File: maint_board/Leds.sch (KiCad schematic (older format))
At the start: 20 parts

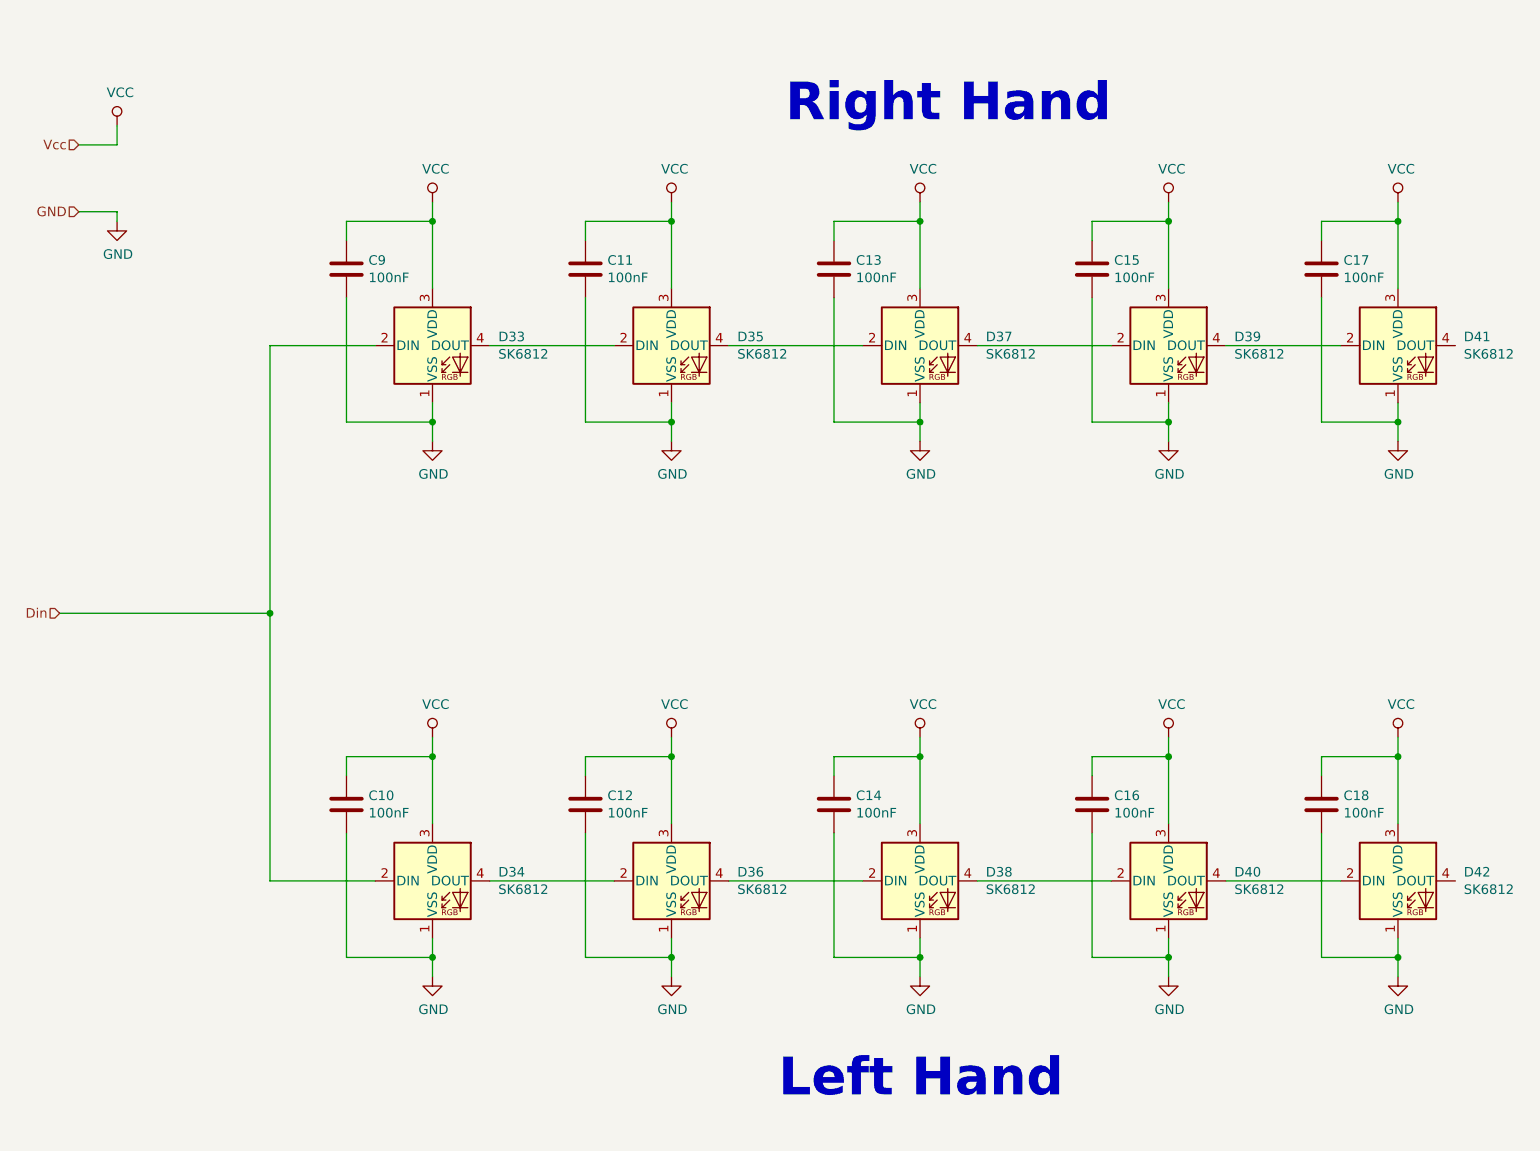
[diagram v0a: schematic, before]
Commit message: removed two leds and fixed recet and usb port
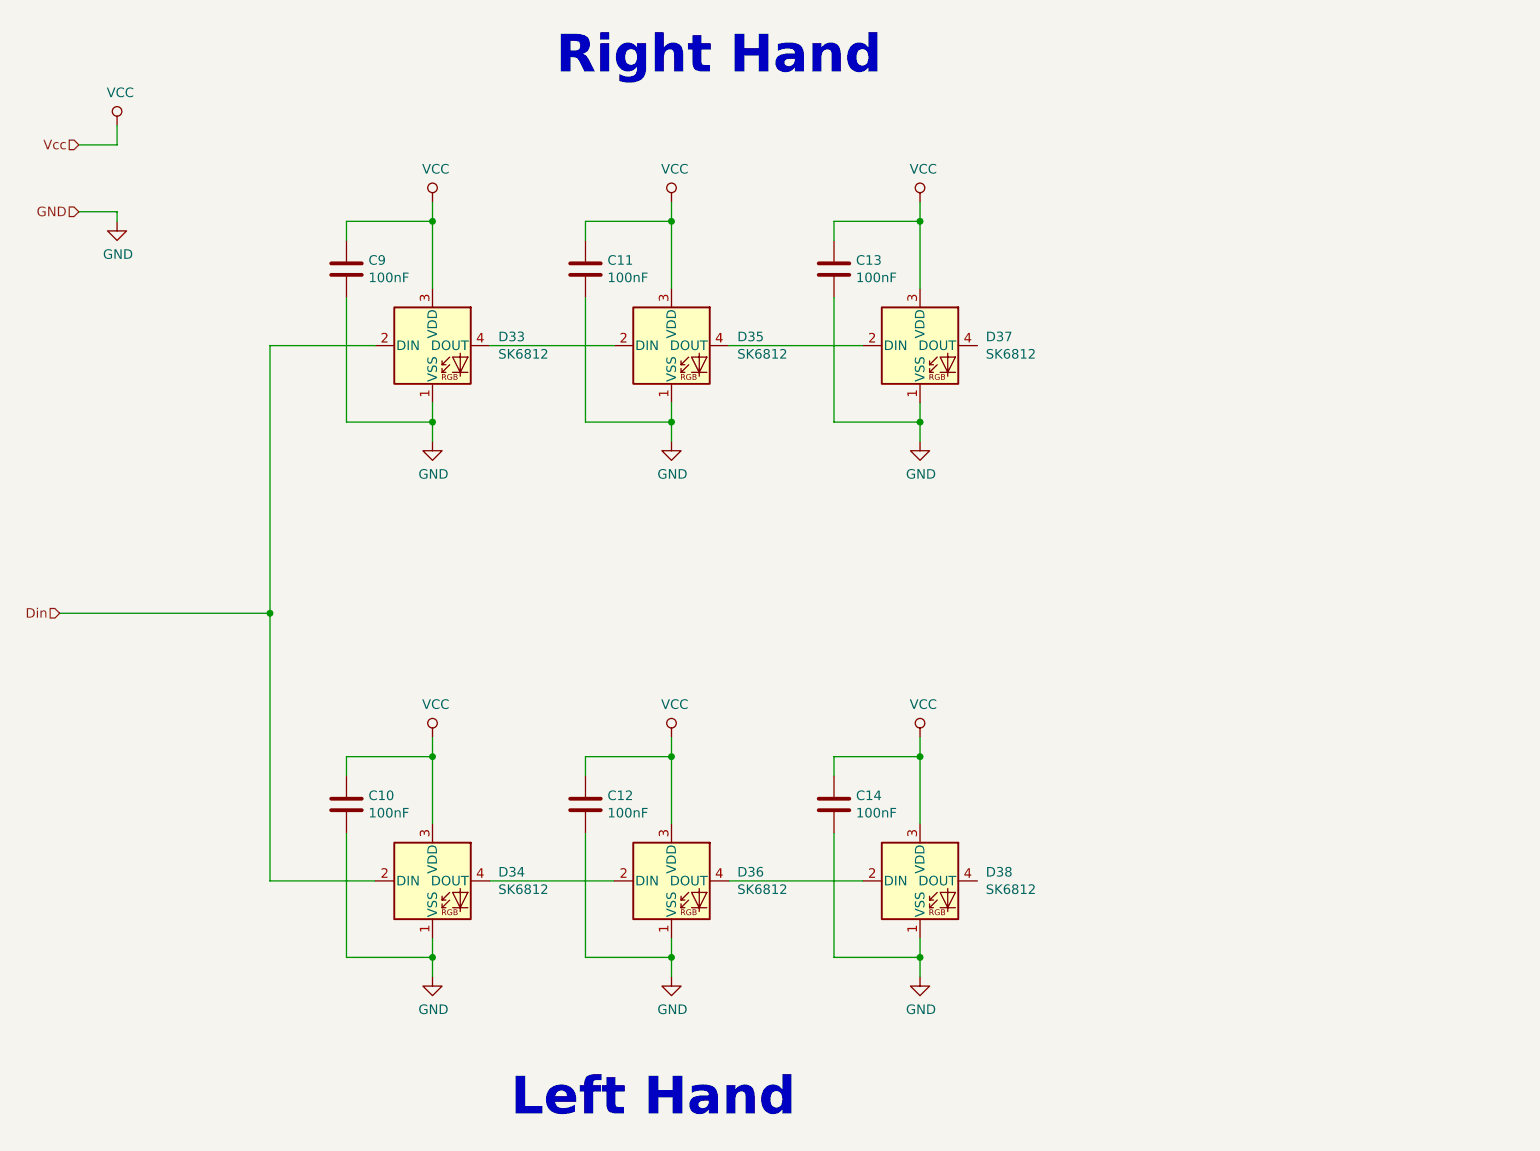
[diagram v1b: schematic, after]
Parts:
- removed C15, C16, C17, C18: 100nF, keyboard_parts:C_1608, symbol Device:C
- removed D39, D40, D41, D42: SK6812, LED_SMD:LED_SK6812_PLCC4_5.0x5.0mm_P3.2mm, symbol LED:SK6812

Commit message: this is before I switch to usb C
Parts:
- removed C13, C14: 100nF, keyboard_parts:C_1608, symbol Device:C
- removed D37, D38: SK6812, LED_SMD:LED_SK6812_PLCC4_5.0x5.0mm_P3.2mm, symbol LED:SK6812
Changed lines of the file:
@@
 $Descr A4 11693 8268
 encoding utf-8
-Sheet 4 4
+Sheet 3 4
 Title ""
 Date ""
@@
 F 3 "https://cdn-shop.adafruit.com/product-files/1138/SK6812+LED+datasheet+.pdf" H 4700 4925 50  0001 L TNN
 	1    4600 5300
-	1    0    0    -1
-$EndComp
-$Comp
-L LED:SK6812 D38
-U 1 1 6020E8F9
-P 5900 5300
-F 0 "D38" H 6244 5346 50  0000 L CNN
-F 1 "SK6812" H 6244 5255 50  0000 L CNN
-F 2 "LED_SMD:LED_SK6812_PLCC4_5.0x5.0mm_P3.2mm" H 5950 5000 50  0001 L TNN
-F 3 "https://cdn-shop.adafruit.com/product-files/1138/SK6812+LED+datasheet+.pdf" H 6000 4925 50  0001 L TNN
-	1    5900 5300
 	1    0    0    -1
 $EndComp
@@
 Wire Wire Line
 	3650 5300 4300 5300
-Wire Wire Line
-	4900 5300 5600 5300
 Text HLabel 1400 3900 0    50   Input ~ 0
 Din
@@
 $EndComp
 $Comp
-L power:VCC #PWR?
-U 1 1 602548C6
-P 5900 4550
-AR Path="/602548C6" Ref="#PWR?"  Part="1"
-AR Path="/6012B71A/602548C6" Ref="#PWR?"  Part="1"
-AR Path="/601EDEE5/602548C6" Ref="#PWR040"  Part="1"
-F 0 "#PWR040" H 5900 4400 50  0001 C CNN
-F 1 "VCC" H 5917 4723 50  0000 C CNN
-F 2 "" H 5900 4550 50  0001 C CNN
-F 3 "" H 5900 4550 50  0001 C CNN
-	1    5900 4550
-	1    0    0    -1
-$EndComp
-$Comp
 L power:GND #PWR?
 U 1 1 6025FF9C
@@
 	1    0    0    -1
 $EndComp
-$Comp
-L power:GND #PWR?
-U 1 1 6025FFA8
-P 5900 5800
-AR Path="/6025FFA8" Ref="#PWR?"  Part="1"
-AR Path="/6012B71A/6025FFA8" Ref="#PWR?"  Part="1"
-AR Path="/601EDEE5/6025FFA8" Ref="#PWR041"  Part="1"
-F 0 "#PWR041" H 5900 5550 50  0001 C CNN
-F 1 "GND" H 5905 5627 50  0000 C CNN
-F 2 "" H 5900 5800 50  0001 C CNN
-F 3 "" H 5900 5800 50  0001 C CNN
-	1    5900 5800
-	1    0    0    -1
-$EndComp
-Wire Wire Line
-	5900 5600 5900 5700
 Wire Wire Line
 	4600 5600 4600 5700
@@
 	1    0    0    -1
 $EndComp
-$Comp
-L Device:C C14
-U 1 1 60268AF3
-P 5450 4900
-F 0 "C14" H 5565 4946 50  0000 L CNN
-F 1 "100nF" H 5565 4855 50  0000 L CNN
-F 2 "keyboard_parts:C_1608" H 5488 4750 50  0001 C CNN
-F 3 "~" H 5450 4900 50  0001 C CNN
-	1    5450 4900
-	1    0    0    -1
-$EndComp
-Wire Wire Line
-	5450 5050 5450 5700
-Wire Wire Line
-	5450 5700 5900 5700
-Connection ~ 5900 5700
-Wire Wire Line
-	5900 5700 5900 5800
 Wire Wire Line
 	4150 5050 4150 5700
@@
 	4600 4550 4600 4650
 Wire Wire Line
-	5900 5000 5900 4650
-Wire Wire Line
 	2900 4750 2900 4650
 Wire Wire Line
@@
 Wire Wire Line
 	4600 4650 4600 5000
-Wire Wire Line
-	5450 4750 5450 4650
-Wire Wire Line
-	5450 4650 5900 4650
-Connection ~ 5900 4650
-Wire Wire Line
-	5900 4650 5900 4550
 $Comp
 L LED:SK6812 D33
@@
 	1    0    0    -1
 $EndComp
-$Comp
-L LED:SK6812 D37
-U 1 1 602A2274
-P 5900 2500
-F 0 "D37" H 6244 2546 50  0000 L CNN
-F 1 "SK6812" H 6244 2455 50  0000 L CNN
-F 2 "LED_SMD:LED_SK6812_PLCC4_5.0x5.0mm_P3.2mm" H 5950 2200 50  0001 L TNN
-F 3 "https://cdn-shop.adafruit.com/product-files/1138/SK6812+LED+datasheet+.pdf" H 6000 2125 50  0001 L TNN
-	1    5900 2500
-	1    0    0    -1
-$EndComp
 Wire Wire Line
 	3650 2500 4300 2500
-Wire Wire Line
-	4900 2500 5600 2500
 Wire Wire Line
 	3050 2500 2500 2500
@@
 $EndComp
 $Comp
-L power:VCC #PWR?
-U 1 1 602A229E
-P 5900 1750
-AR Path="/602A229E" Ref="#PWR?"  Part="1"
-AR Path="/6012B71A/602A229E" Ref="#PWR?"  Part="1"
-AR Path="/601EDEE5/602A229E" Ref="#PWR038"  Part="1"
-F 0 "#PWR038" H 5900 1600 50  0001 C CNN
-F 1 "VCC" H 5917 1923 50  0000 C CNN
-F 2 "" H 5900 1750 50  0001 C CNN
-F 3 "" H 5900 1750 50  0001 C CNN
-	1    5900 1750
-	1    0    0    -1
-$EndComp
-$Comp
 L power:GND #PWR?
 U 1 1 602A22AA
@@
 	1    0    0    -1
 $EndComp
-$Comp
-L power:GND #PWR?
-U 1 1 602A22B6
-P 5900 3000
-AR Path="/602A22B6" Ref="#PWR?"  Part="1"
-AR Path="/6012B71A/602A22B6" Ref="#PWR?"  Part="1"
-AR Path="/601EDEE5/602A22B6" Ref="#PWR039"  Part="1"
-F 0 "#PWR039" H 5900 2750 50  0001 C CNN
-F 1 "GND" H 5905 2827 50  0000 C CNN
-F 2 "" H 5900 3000 50  0001 C CNN
-F 3 "" H 5900 3000 50  0001 C CNN
-	1    5900 3000
-	1    0    0    -1
-$EndComp
-Wire Wire Line
-	5900 2800 5900 2900
 Wire Wire Line
 	4600 2800 4600 2900
@@
 	1    0    0    -1
 $EndComp
-$Comp
-L Device:C C13
-U 1 1 602A22D9
-P 5450 2100
-F 0 "C13" H 5565 2146 50  0000 L CNN
-F 1 "100nF" H 5565 2055 50  0000 L CNN
-F 2 "keyboard_parts:C_1608" H 5488 1950 50  0001 C CNN
-F 3 "~" H 5450 2100 50  0001 C CNN
-	1    5450 2100
-	1    0    0    -1
-$EndComp
-Wire Wire Line
-	5450 2250 5450 2900
-Wire Wire Line
-	5450 2900 5900 2900
-Connection ~ 5900 2900
-Wire Wire Line
-	5900 2900 5900 3000
 Wire Wire Line
 	4150 2250 4150 2900
@@
 	4600 1750 4600 1850
 Wire Wire Line
-	5900 2200 5900 1850
-Wire Wire Line
 	2900 1950 2900 1850
 Wire Wire Line
@@
 Wire Wire Line
 	4600 1850 4600 2200
-Wire Wire Line
-	5450 1950 5450 1850
-Wire Wire Line
-	5450 1850 5900 1850
-Connection ~ 5900 1850
-Wire Wire Line
-	5900 1850 5900 1750
 Text Notes 5700 1100 2    197  ~ 39
 Right Hand
